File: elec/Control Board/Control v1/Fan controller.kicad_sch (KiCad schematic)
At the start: 0 parts

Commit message: added labels for heiarchy sheets, and first pass on basic control interface circuits
Signed-off-by: lokimetasmith <lokimail@gmail.com>
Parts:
- added D1: BZV55B3V3, Diode_SMD:D_MiniMELF, symbol Diode:BZV55B3V3
- added J3: Conn_01x04_Pin, symbol Connector:Conn_01x04_Pin
- added Q2: Q_NMOS_GDS, symbol Device:Q_NMOS_GDS
- added R2, R3, R4: 10k, symbol Device:R
- added R5: 4k7, symbol Device:R
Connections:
- new net: J3.2 (Pin_2), Q2.3 (S)
- new net: J3.3 (Pin_3), R3.2, R4.2
- new net +24V: Q2.2 (D), R3.1
- new net FAN_PWM: D1.1 (K), J3.4 (Pin_4)
- new net FAN_TACH: R4.1, R5.1
- new net Fan_EN: Q2.1 (G), R2.1
- new net GND: J3.1 (Pin_1), R2.2, R5.2

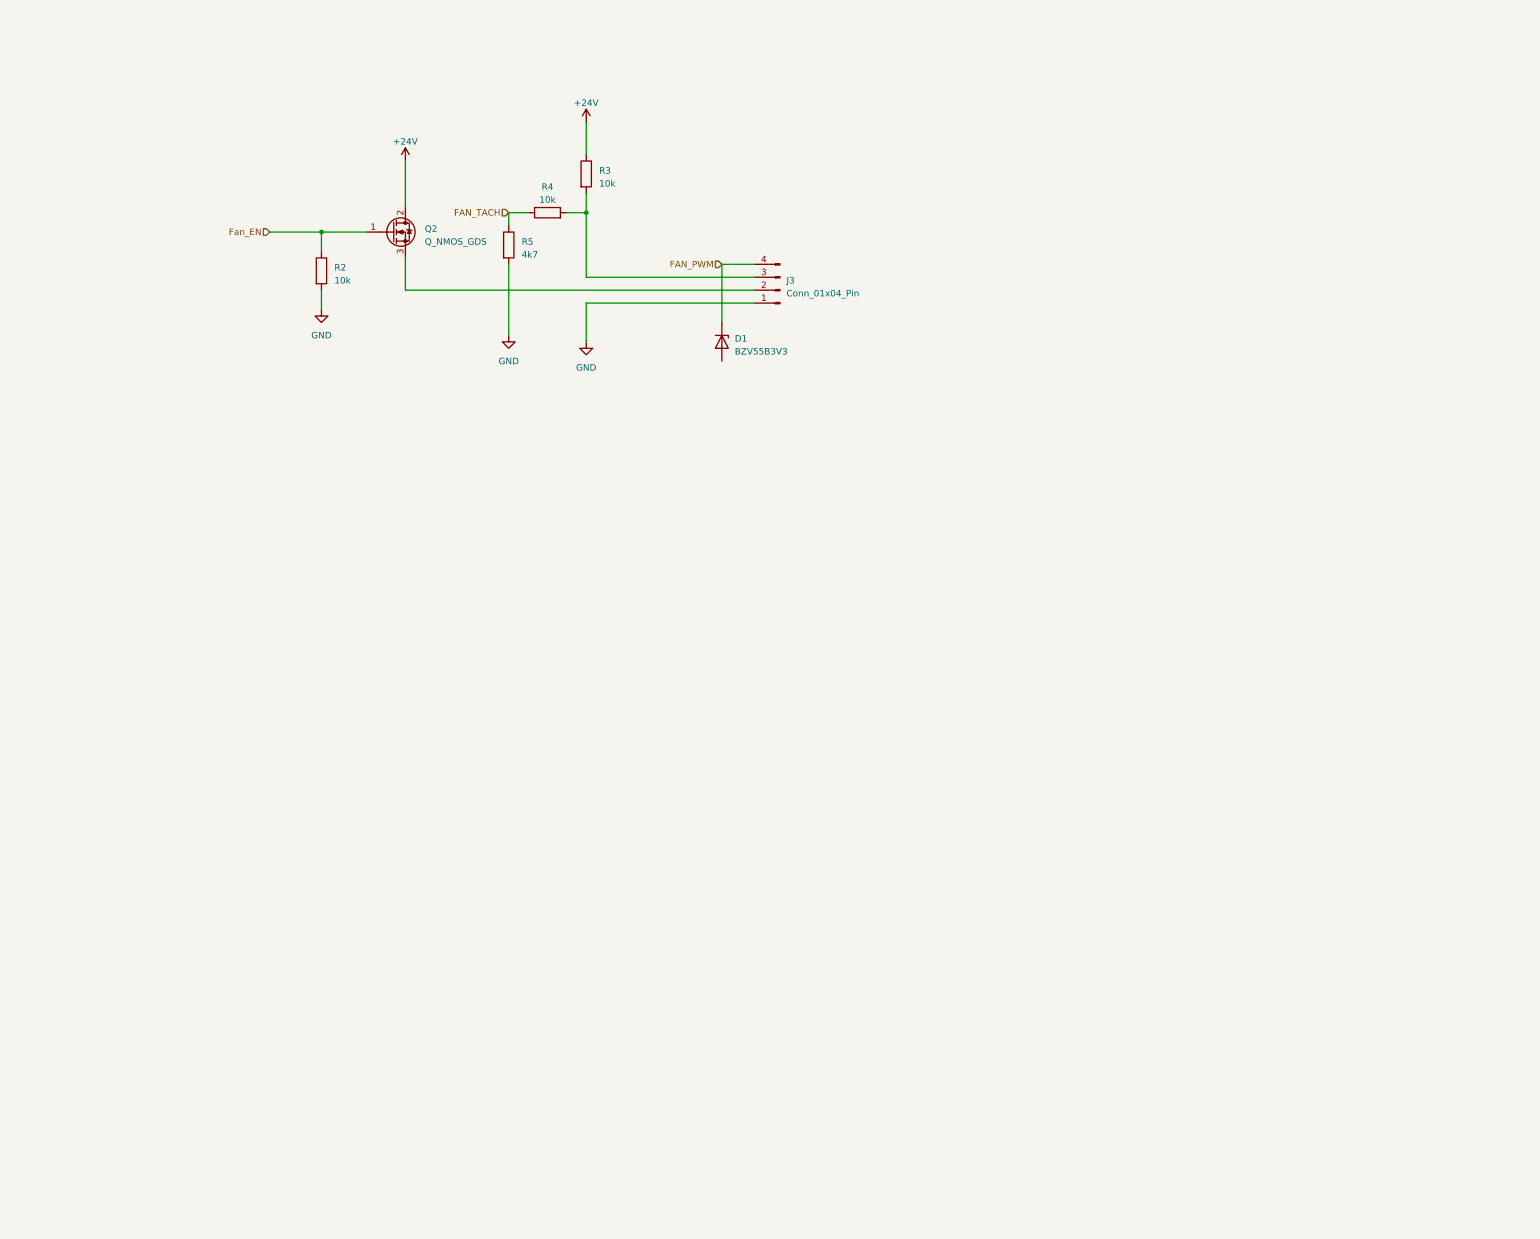
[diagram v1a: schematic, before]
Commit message: imported Lee's changed inputs into the folder Control Board,
Also added in Robert's pin labels

ToDo: clean up broken links, and import in the layout files from Lee's project

Clean up the fan control pinout, the DB25 is a bit of a mess
consider using IDC to DB25 connectors for ease of assembly and installation.


Signed-off-by: lokimetasmith <lokimail@gmail.com>
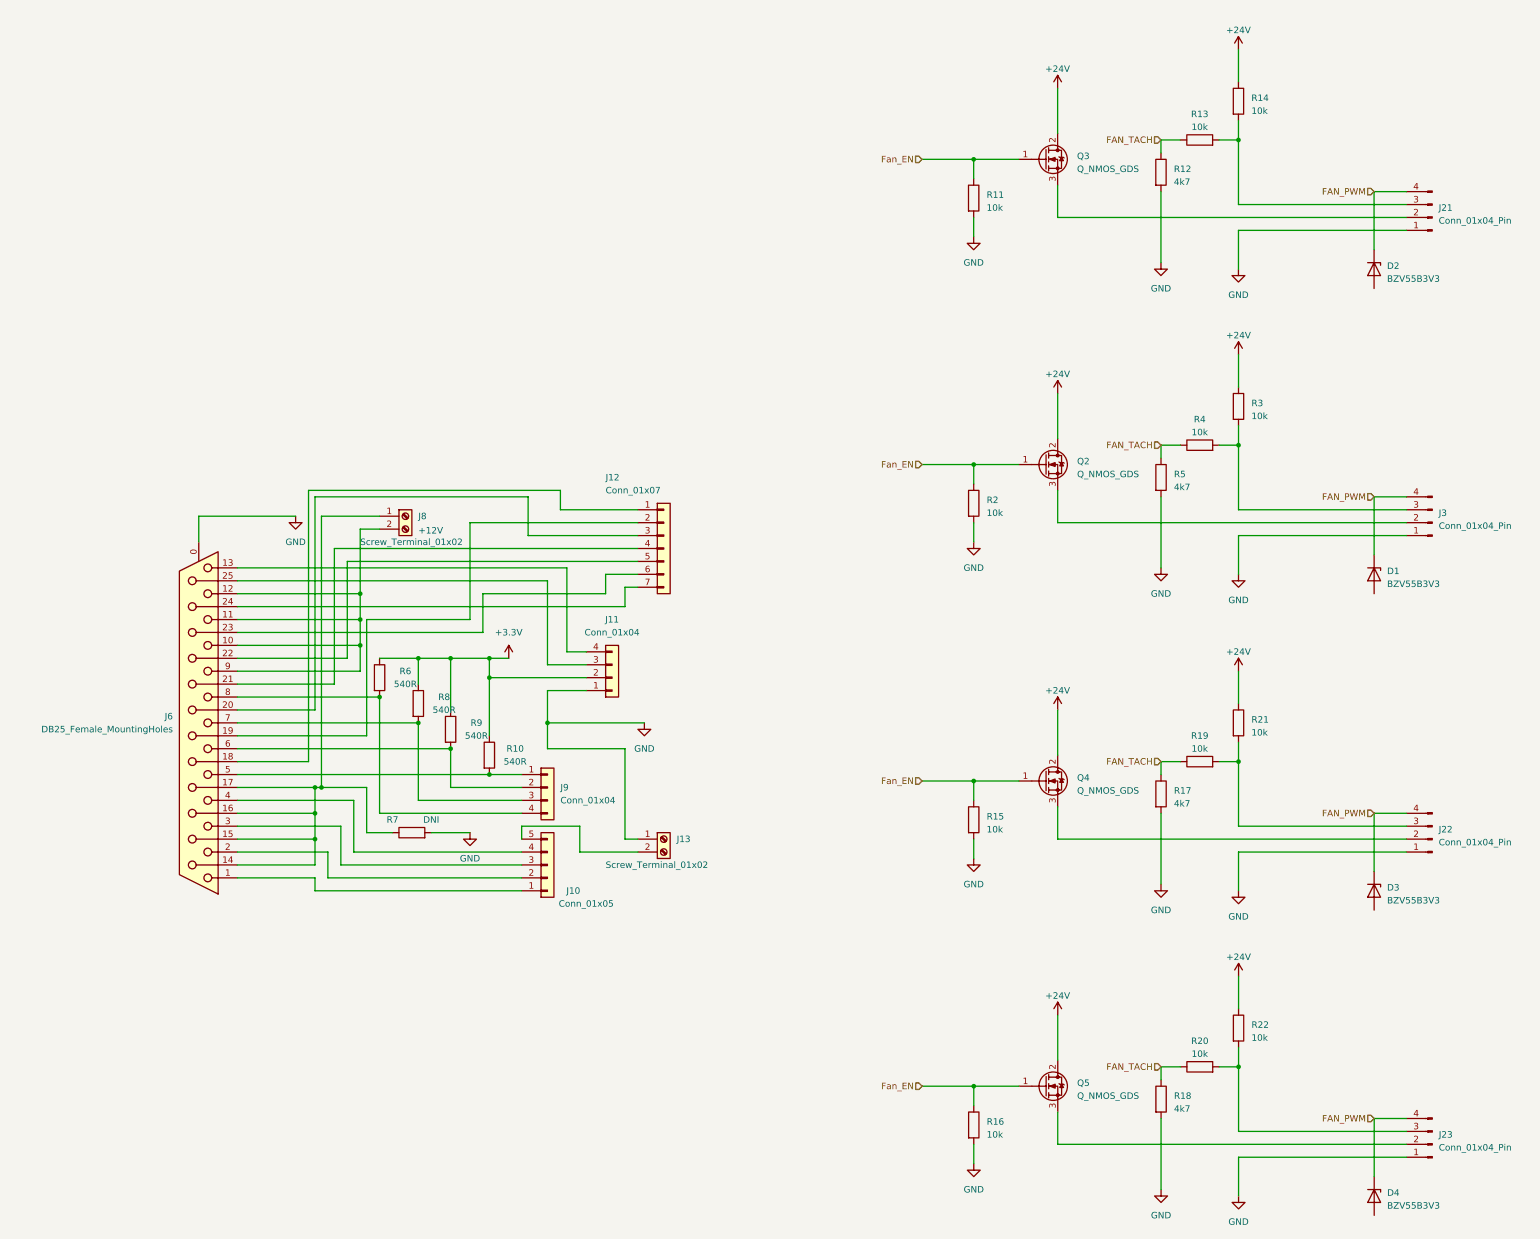
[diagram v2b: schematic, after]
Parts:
- added D2, D3, D4: BZV55B3V3, Diode_SMD:D_MiniMELF, symbol Diode:BZV55B3V3
- added J10: Conn_01x05, Connector_PinHeader_2.54mm:PinHeader_1x05_P2.54mm_Vertical, symbol Connector_Generic:Conn_01x05
- added J11, J9: Conn_01x04, Connector_PinHeader_2.54mm:PinHeader_1x04_P2.54mm_Vertical, symbol Connector_Generic:Conn_01x04
- added J12: Conn_01x07, Connector_PinHeader_2.54mm:PinHeader_1x07_P2.54mm_Vertical, symbol Connector_Generic:Conn_01x07
- added J13, J8: Screw_Terminal_01x02, TerminalBlock_MetzConnect:TerminalBlock_MetzConnect_Type073_RT02602HBLU_1x02_P5.08mm_Horizontal, symbol Connector:Screw_Terminal_01x02
- added J21, J22, J23: Conn_01x04_Pin, symbol Connector:Conn_01x04_Pin
- added J6: DB25_Female_MountingHoles, Connector_Dsub:DSUB-25_Female_Horizontal_P2.77x2.84mm_EdgePinOffset4.94mm_Housed_MountingHolesOffset7.48mm, symbol Connector:DB25_Female_MountingHoles
- added Q3, Q4, Q5: Q_NMOS_GDS, symbol Device:Q_NMOS_GDS
- added R10, R6, R8, R9: 540R, Resistor_SMD:R_0603_1608Metric_Pad0.98x0.95mm_HandSolder, symbol Device:R
- added R11, R13, R14, R15, R16, R19, R20, R21, R22: 10k, symbol Device:R
- added R12, R17, R18: 4k7, symbol Device:R
- added R7: DNI, Resistor_SMD:R_0603_1608Metric_Pad0.98x0.95mm_HandSolder, symbol Device:R
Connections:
- net +24V: now also Q3.2 (D), Q4.2 (D), Q5.2 (D), R14.1, R21.1, R22.1
- net FAN_PWM: now also D2.1 (K), D3.1 (K), D4.1 (K), J21.4 (Pin_4), J22.4 (Pin_4), J23.4 (Pin_4)
- net FAN_TACH: now also R12.1, R13.1, R17.1, R18.1, R19.1, R20.1
- net Fan_EN: now also Q3.1 (G), Q4.1 (G), Q5.1 (G), R11.1, R15.1, R16.1
- net GND: now also J11.1 (Pin_1), J13.1 (Pin_1), J21.1 (Pin_1), J22.1 (Pin_1), J23.1 (Pin_1), J6.0 (PAD), R11.2, R12.2, R15.2, R16.2, R17.2, R18.2, R7.2
- new net: J6.8, J9.4 (Pin_4), R6.2
- new net: J23.2 (Pin_2), Q5.3 (S)
- new net: J23.3 (Pin_3), R20.2, R22.2
- new net: J6.5, J9.1 (Pin_1), R10.2
- new net: J6.6, J9.2 (Pin_2), R9.2
- new net: J21.3 (Pin_3), R13.2, R14.2
- new net: J6.14 (P14), J6.15 (P15), J6.16 (P16), J6.17 (P17), J8.1 (Pin_1), R7.1
- new net: J6.7, J9.3 (Pin_3), R8.2
- new net: J21.2 (Pin_2), Q3.3 (S)
- new net: J6.10, J6.11, J6.12, J6.9, J8.2 (Pin_2)
- new net: J22.2 (Pin_2), Q4.3 (S)
- new net: J22.3 (Pin_3), R19.2, R21.2
- new net: J10.5 (Pin_5), J13.2 (Pin_2)
- new net: J11.3 (Pin_3), J6.25 (P25)
- new net: J11.4 (Pin_4), J6.13
- new net: J10.1 (Pin_1), J6.1
- new net: J10.2 (Pin_2), J6.2
- new net: J10.3 (Pin_3), J6.3
- new net: J10.4 (Pin_4), J6.4
- new net: J12.1 (Pin_1), J6.18 (P18)
- new net: J12.2 (Pin_2), J6.19 (P19)
- new net: J12.3 (Pin_3), J6.20 (P20)
- new net: J12.4 (Pin_4), J6.21 (P21)
- new net: J12.5 (Pin_5), J6.22 (P22)
- new net: J12.6 (Pin_6), J6.23 (P23)
- new net: J12.7 (Pin_7), J6.24 (P24)
- new net +3.3V: J11.2 (Pin_2), R10.1, R6.1, R8.1, R9.1
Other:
- note added: "+12V"
- moved on the sheet: D1, J3, Q2, R2, R3, R4, R5

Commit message: Switch to FAN POWER.
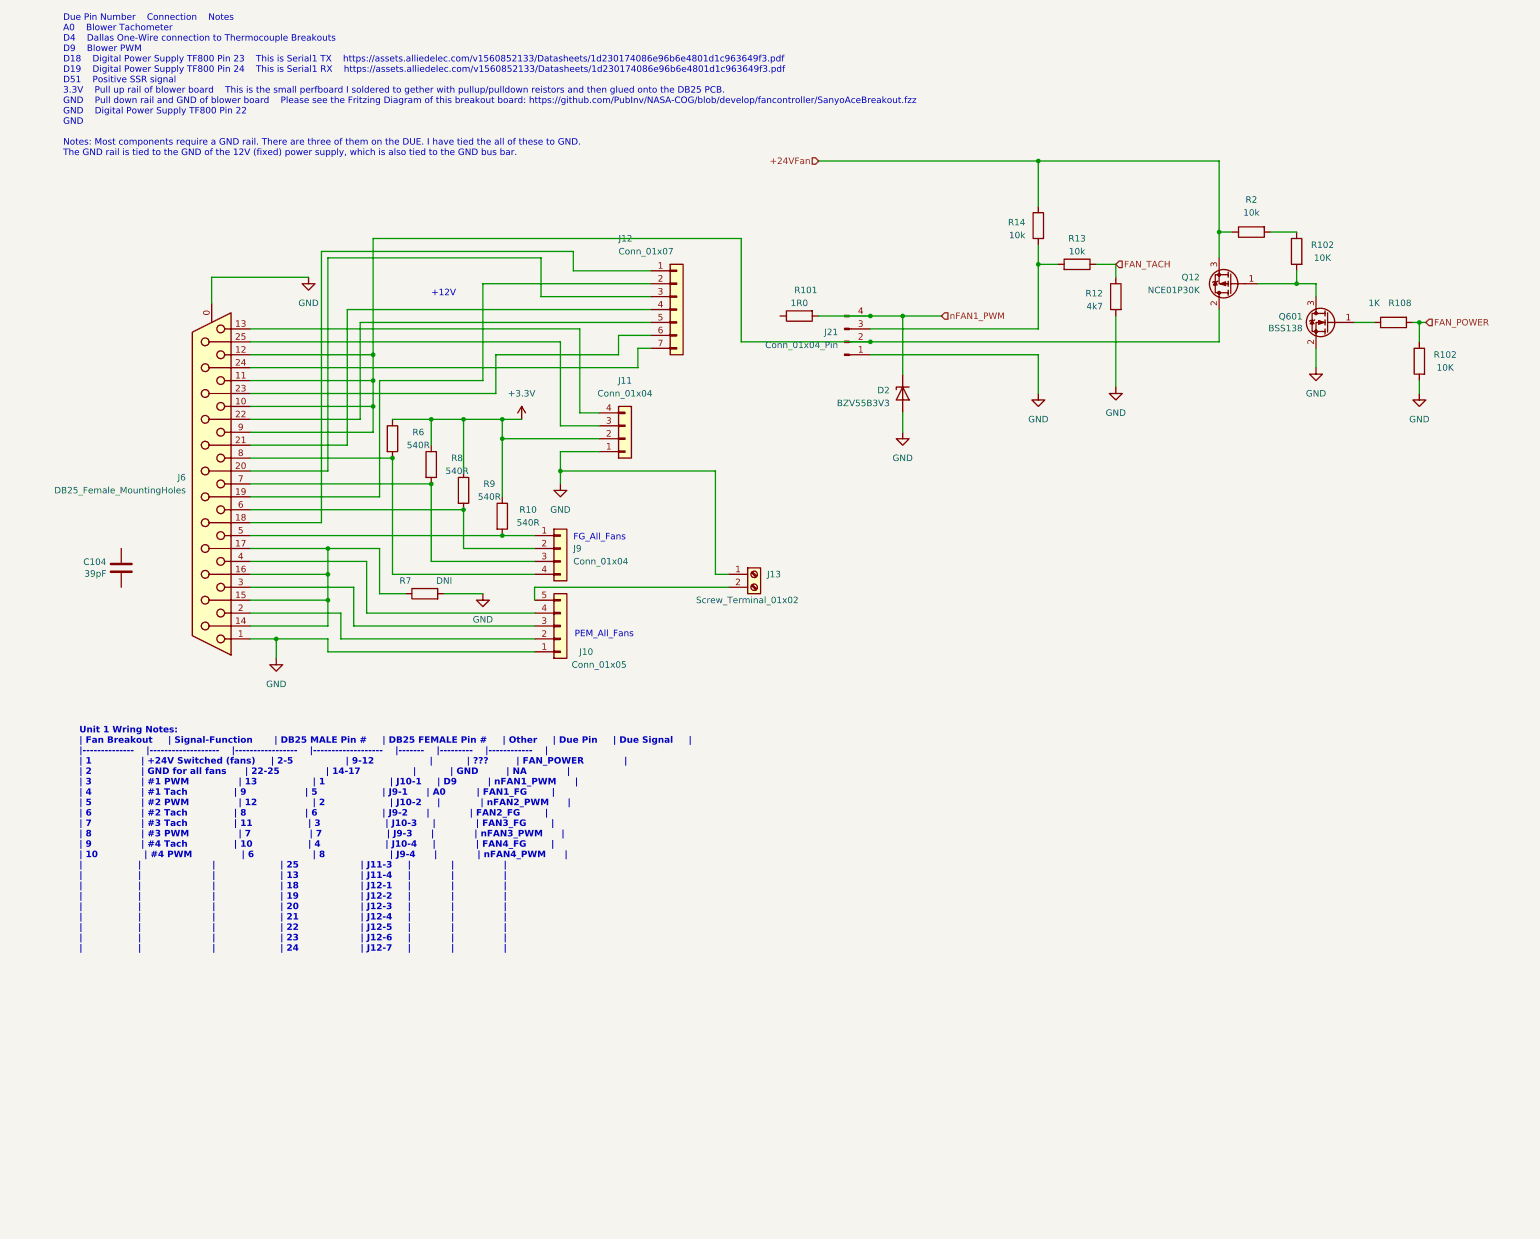
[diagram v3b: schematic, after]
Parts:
- removed D1, D3, D4: BZV55B3V3, Diode_SMD:D_MiniMELF, symbol Diode:BZV55B3V3
- removed J22, J23, J3: Conn_01x04_Pin, symbol Connector:Conn_01x04_Pin
- removed J8: Screw_Terminal_01x02, TerminalBlock_MetzConnect:TerminalBlock_MetzConnect_Type073_RT02602HBLU_1x02_P5.08mm_Horizontal, symbol Connector:Screw_Terminal_01x02
- removed Q2, Q3, Q4, Q5: Q_NMOS_GDS, symbol Device:Q_NMOS_GDS
- removed R11, R15, R16, R19, R20, R21, R22, R3, R4: 10k, symbol Device:R
- removed R17, R18, R5: 4k7, symbol Device:R
- added C104: 39pF, Capacitor_SMD:C_0603_1608Metric_Pad1.08x0.95mm_HandSolder, symbol Device:C
- added Q12: NCE01P30K, Package_TO_SOT_SMD:TO-252-2, symbol Transistor_FET:SUD45P03-09
- added Q601: BSS138, Package_TO_SOT_SMD:SOT-23, symbol Transistor_FET:BSS138
- added R101: 1R0, Resistor_SMD:R_0603_1608Metric_Pad0.98x0.95mm_HandSolder, symbol Device:R
- added R102 (x2): 10K, Resistor_SMD:R_0603_1608Metric_Pad0.98x0.95mm_HandSolder, symbol Device:R
- added R108: 1K, Resistor_SMD:R_0603_1608Metric_Pad0.98x0.95mm_HandSolder, symbol Device:R
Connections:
- net Fan_EN is gone; now on net +24VFan: R2.1
- net GND: now also D2.2 (A), J10.1 (Pin_1), J6.1, Q601.2 (S), R102.2; no longer R2.2
- net at J21.2 (Pin_2): now also J6.10, J6.11, J6.12, J6.9, Q12.2 (D)
- net +24V renamed +24VFan
- net +24VFan: now also Q12.3 (S)
- net FAN_PWM renamed nFAN1_PWM
- net nFAN1_PWM: now also R101.2
- new net: R102.1, R2.2
- new net: Q12.1 (G), Q601.3 (D), R102.2
- new net: Q601.1 (G), R108.1
- new net FAN_POWER: R102.1, R108.2
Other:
- note added: "Due Pin Number Connection Notes A0 Blower Tachometer D4 Dallas One-Wire connection to Thermocouple Breakouts D9 Blower PWM D18 Digital Power Supply TF800 Pin 23 This is Serial1 TX https://assets.alliedelec.com/v1560852133/Datasheets/1d230174086e96b6e4801d1c963649f3.pdf D19 Digital Power Supply TF800 Pin 24 This is Serial1 RX https://assets.alliedelec.com/v1560852133/Datasheets/1d230174086e96b6e48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"
- note added: "FG_All_Fans"
- note added: "PEM_All_Fans"
- note added: "Unit 1 Wring Notes: | Fan Breakout | Signal-Function | DB25 MALE Pin # | DB25 FEMALE Pin # | Other | Due Pin | Due Signal | |-------------- |------------------- |----------------- |------------------- |------- |--------- |------------ | | 1 | +24V Switched (fans) | 2-5 | 9-12 | | ??? | FAN_POWER | | 2 | GND for all fans | 22-25 | 14-17 | | GND | NA | | 3 | #1 PWM | 13 | 1 | J10-1 | D9 | nFAN1_PWM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"
- moved on the sheet: D2, J10, J11, J12, J13, J21, J6, J9, R10, R12, R13, R14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
